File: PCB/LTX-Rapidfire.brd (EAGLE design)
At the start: 62.2 x 46.7 mm, 51 parts, among them J1 F-1X08-SIP-100-40Y, Q1 2N3904, Q10 SS8550D, Q11 2N3906, Q12 2N3906, Q13 2N3904, Q2 2N3906, Q3 2N3904, Q4 2N3904, Q5 2N3904, Q6 2N3906, Q7 2N3906, Q8 2N3906, Q9 2N3904, SW1 F-1X02-SIP-100-40, U2 Z8F082ADIL-8

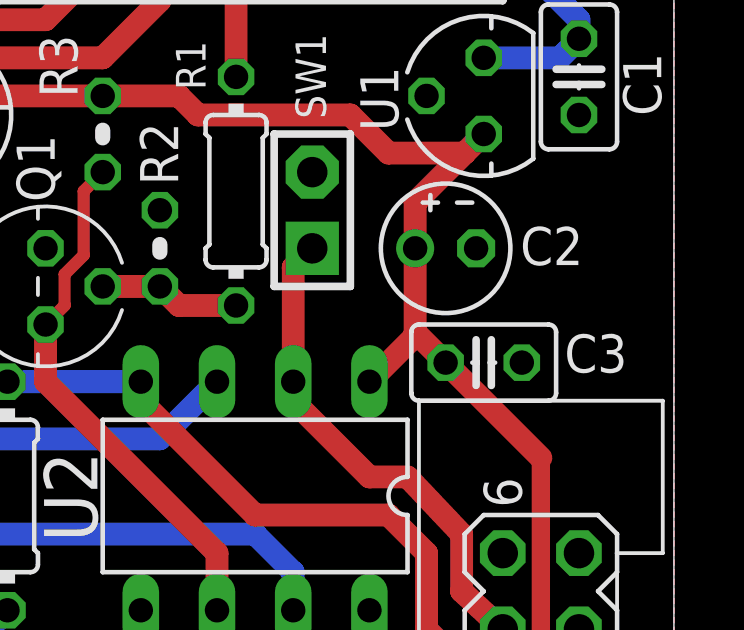
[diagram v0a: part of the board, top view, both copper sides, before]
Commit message: A resistor got missed! Whoops. Put that back in...
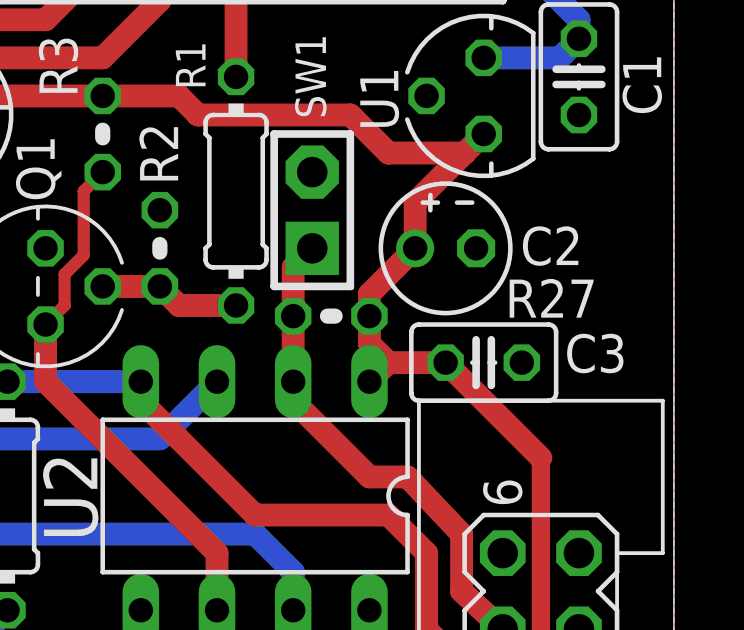
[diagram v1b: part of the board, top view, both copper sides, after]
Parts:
- added R27: 10k, rcl:0204V
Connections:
- net PA0: now also R27.1
- net VCC: now also R27.2
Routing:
- net VCC: track 103.8 -> 104.8 mm
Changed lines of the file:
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@@
 <attribute name="NAME" x="8.509" y="10.3632" size="1.27" layer="25" ratio="10" rot="R180"/>
+</element>
+<element name="R27" library="rcl" package="0204V" value="10k" x="50.8" y="27.2542" smashed="yes">
+<attribute name="NAME" x="56.5912" y="27.2034" size="1.27" layer="25" ratio="10"/>
 </element>
 </elements>
@@
 <wire x1="55.245" y1="32.6898" x2="53.594" y2="31.0388" width="0.762" layer="1"/>
 <wire x1="53.594" y1="31.0388" x2="53.594" y2="29.5148" width="0.762" layer="1"/>
-<wire x1="54.61" y1="25.7048" x2="53.594" y2="26.7208" width="0.762" layer="1"/>
-<wire x1="53.594" y1="26.7208" x2="53.594" y2="29.5148" width="0.762" layer="1"/>
-<wire x1="52.07" y1="25.0698" x2="53.594" y2="26.5938" width="0.762" layer="1"/>
-<wire x1="53.594" y1="26.5938" x2="53.594" y2="26.7208" width="0.762" layer="1"/>
 <wire x1="54.61" y1="25.7048" x2="57.785" y2="22.5298" width="0.762" layer="1"/>
 <wire x1="57.785" y1="22.5298" x2="57.785" y2="15.5448" width="0.6096" layer="1"/>
@@
 <wire x1="59.055" y1="7.9248" x2="56.515" y2="5.3848" width="0.762" layer="1"/>
 <wire x1="56.515" y1="5.3848" x2="56.515" y2="3.4798" width="0.762" layer="1"/>
+<contactref element="R27" pad="2"/>
+<wire x1="54.61" y1="25.7048" x2="52.705" y2="25.7048" width="0.762" layer="1"/>
+<wire x1="52.705" y1="25.7048" x2="52.07" y2="25.0698" width="0.762" layer="1"/>
+<wire x1="52.07" y1="27.2542" x2="52.07" y2="26.3398" width="0.762" layer="1"/>
+<wire x1="52.07" y1="26.3398" x2="52.705" y2="25.7048" width="0.762" layer="1"/>
+<wire x1="52.07" y1="27.2542" x2="52.07" y2="27.9908" width="0.762" layer="1"/>
+<wire x1="52.07" y1="27.9908" x2="53.594" y2="29.5148" width="0.762" layer="1"/>
 </signal>
 <signal name="N$2">
@@
 <contactref element="U2" pad="2"/>
 <contactref element="J2" pad="4"/>
-<wire x1="49.53" y1="25.0698" x2="49.53" y2="28.8798" width="0.762" layer="1"/>
-<wire x1="49.53" y1="28.8798" x2="50.165" y2="29.5148" width="0.762" layer="1"/>
 <wire x1="49.53" y1="25.0698" x2="49.53" y2="24.4348" width="0.762" layer="1"/>
 <wire x1="49.53" y1="24.4348" x2="52.07" y2="21.8948" width="0.762" layer="1"/>
@@
 <wire x1="55.1434" y1="19.9898" x2="55.1434" y2="18.0848" width="0.762" layer="1"/>
 <wire x1="55.1434" y1="18.0848" x2="56.515" y2="16.8148" width="0.762" layer="1"/>
+<contactref element="R27" pad="1"/>
+<wire x1="49.53" y1="25.0698" x2="49.53" y2="27.2542" width="0.762" layer="1"/>
+<wire x1="49.53" y1="27.2542" x2="49.53" y2="28.8798" width="0.762" layer="1"/>
+<wire x1="49.53" y1="28.8798" x2="50.165" y2="29.5148" width="0.762" layer="1"/>
 </signal>
 <signal name="N$17">

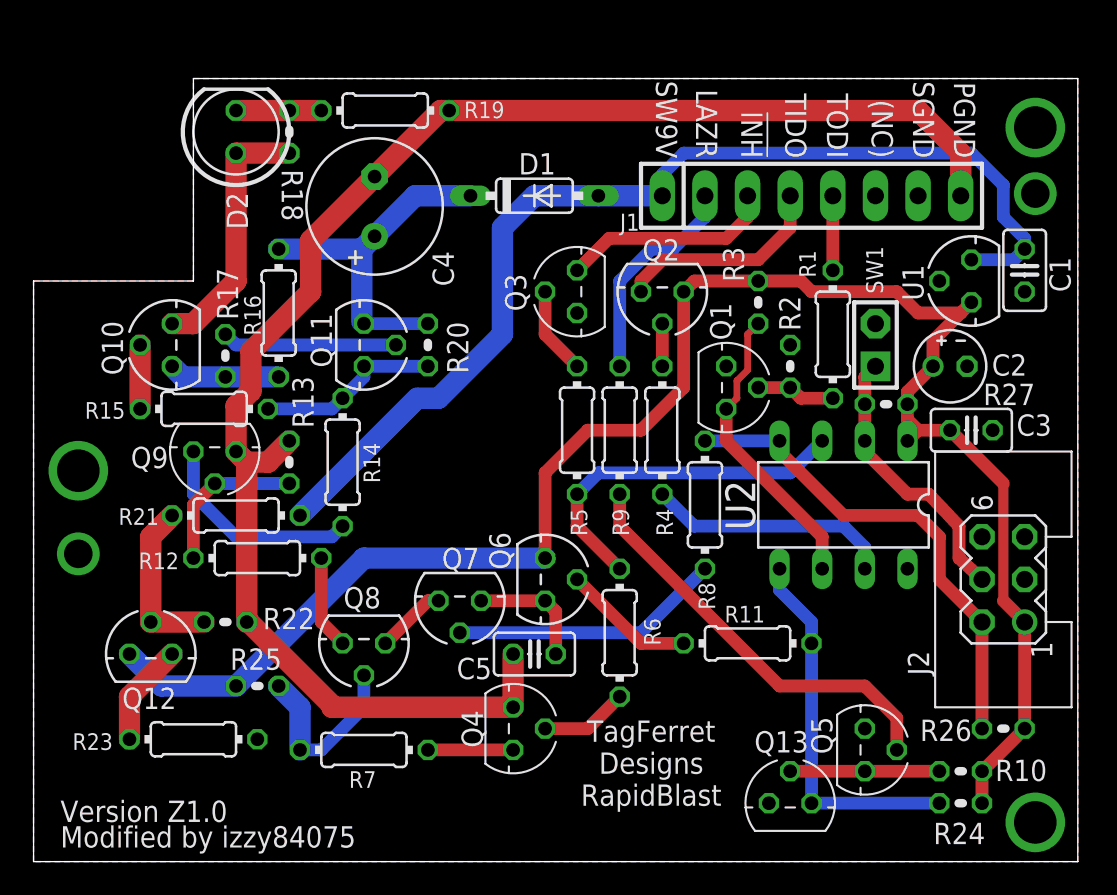
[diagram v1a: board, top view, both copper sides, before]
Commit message: Replace R19 out so you can fit a 1/2W resistor in.
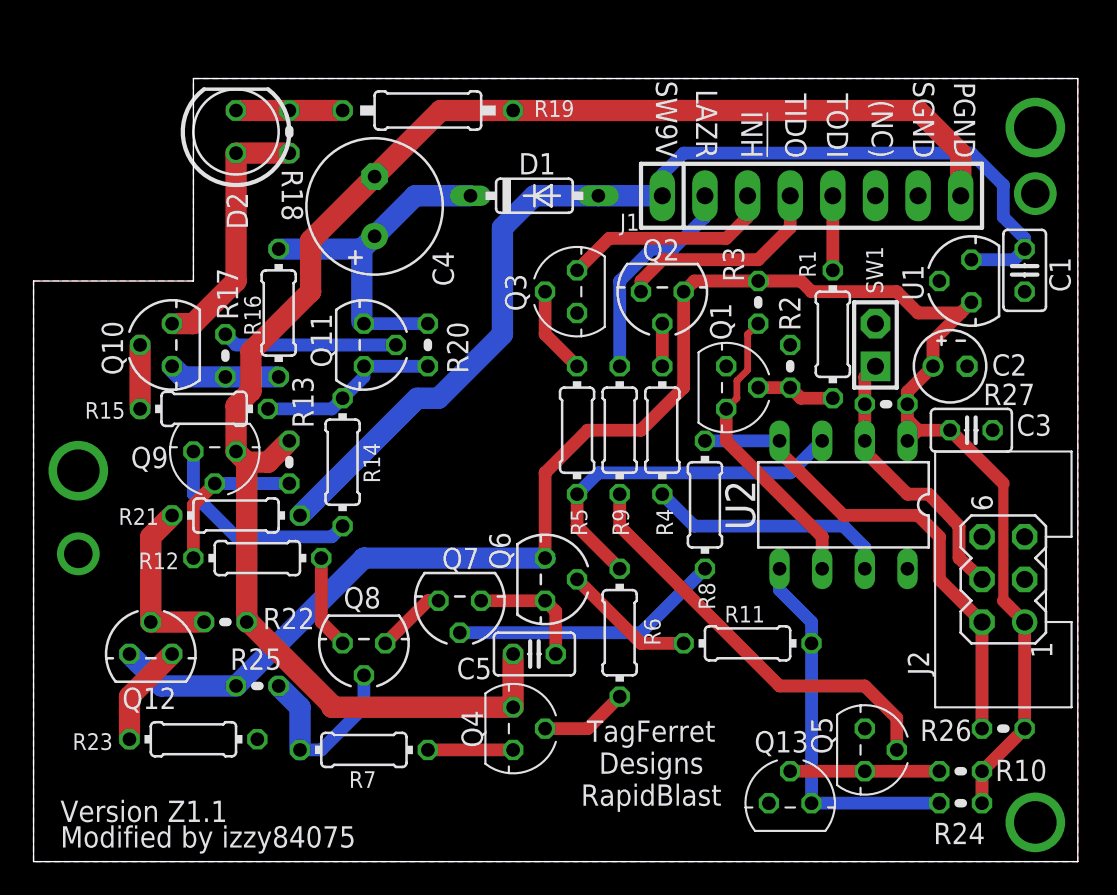
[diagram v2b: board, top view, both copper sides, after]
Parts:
- R19: device rcl:0204/7 -> rcl:0207/10
- moved R19 2.54 mm to (23.5, 44.8)
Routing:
- net N$7: track 5.08 -> 6.35 mm
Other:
- board text added: "Version Z1.1"
- board text removed: "Version Z1.0"
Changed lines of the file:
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@@
 <layers>
 <layer number="1" name="Top" color="4" fill="1" visible="yes" active="yes"/>
+<layer number="2" name="Route2" color="1" fill="3" visible="no" active="no"/>
+<layer number="3" name="Route3" color="4" fill="3" visible="no" active="no"/>
+<layer number="4" name="Route4" color="1" fill="4" visible="no" active="no"/>
+<layer number="5" name="Route5" color="4" fill="4" visible="no" active="no"/>
+<layer number="6" name="Route6" color="1" fill="8" visible="no" active="no"/>
+<layer number="7" name="Route7" color="4" fill="8" visible="no" active="no"/>
+<layer number="8" name="Route8" color="1" fill="2" visible="no" active="no"/>
+<layer number="9" name="Route9" color="4" fill="2" visible="no" active="no"/>
+<layer number="10" name="Route10" color="1" fill="7" visible="no" active="no"/>
+<layer number="11" name="Route11" color="4" fill="7" visible="no" active="no"/>
+<layer number="12" name="Route12" color="1" fill="5" visible="no" active="no"/>
+<layer number="13" name="Route13" color="4" fill="5" visible="no" active="no"/>
+<layer number="14" name="Route14" color="1" fill="6" visible="no" active="no"/>
+<layer number="15" name="Route15" color="4" fill="6" visible="no" active="no"/>
 <layer number="16" name="Bottom" color="1" fill="1" visible="yes" active="yes"/>
 <layer number="17" name="Pads" color="2" fill="1" visible="yes" active="yes"/>
@@
 Designs
 RapidBlast</text>
-<text x="1.6002" y="2.3622" size="1.27" layer="25" font="vector" rot="SR0">Version Z1.0</text>
+<text x="1.6002" y="2.3622" size="1.27" layer="25" font="vector" rot="SR0">Version Z1.1</text>
 <text x="1.6002" y="0.8382" size="1.27" layer="25" font="vector">Modified by izzy84075</text>
 <wire x1="0" y1="0" x2="62.22" y2="0" width="0" layer="20"/>
@@
 <attribute name="VALUE" x="13.8684" y="46.6852" size="1.27" layer="27" ratio="10" rot="R90"/>
 </element>
-<element name="R19" library="rcl" package="0204/7" value="3.9" x="20.955" y="44.7548" smashed="yes" rot="R180">
-<attribute name="NAME" x="25.654" y="44.2976" size="0.9906" layer="25" ratio="10"/>
+<element name="R19" library="rcl" package="0207/10" value="3.9" x="23.495" y="44.7548" smashed="yes" rot="R180">
+<attribute name="NAME" x="29.8196" y="44.3738" size="0.9906" layer="25" ratio="10"/>
 </element>
 <element name="R13" library="rcl" package="0204V" value="1.3k" x="15.24" y="23.7998" smashed="yes" rot="R90">
@@
 <wire x1="55.245" y1="39.6748" x2="55.245" y2="42.2148" width="1.27" layer="1"/>
 <wire x1="55.245" y1="42.2148" x2="52.705" y2="44.7548" width="1.27" layer="1"/>
-<wire x1="52.705" y1="44.7548" x2="24.765" y2="44.7548" width="1.27" layer="1"/>
-<wire x1="24.765" y1="44.7548" x2="24.257" y2="44.7548" width="1.27" layer="1"/>
+<wire x1="52.705" y1="44.7548" x2="28.575" y2="44.7548" width="1.27" layer="1"/>
+<wire x1="28.575" y1="44.7548" x2="24.257" y2="44.7548" width="1.27" layer="1"/>
 <wire x1="24.257" y1="44.7548" x2="20.32" y2="40.8178" width="1.27" layer="1"/>
 <wire x1="20.32" y1="40.8178" x2="16.51" y2="37.0078" width="1.27" layer="1"/>
@@
 <contactref element="R18" pad="2"/>
 <contactref element="R19" pad="2"/>
-<wire x1="17.145" y1="44.7548" x2="15.24" y2="44.7548" width="1.27" layer="1"/>
+<wire x1="18.415" y1="44.7548" x2="15.24" y2="44.7548" width="1.27" layer="1"/>
 <wire x1="15.24" y1="44.7548" x2="12.065" y2="44.7548" width="1.27" layer="1"/>
 </signal>
